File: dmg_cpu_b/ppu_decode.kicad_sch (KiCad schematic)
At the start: 69 parts

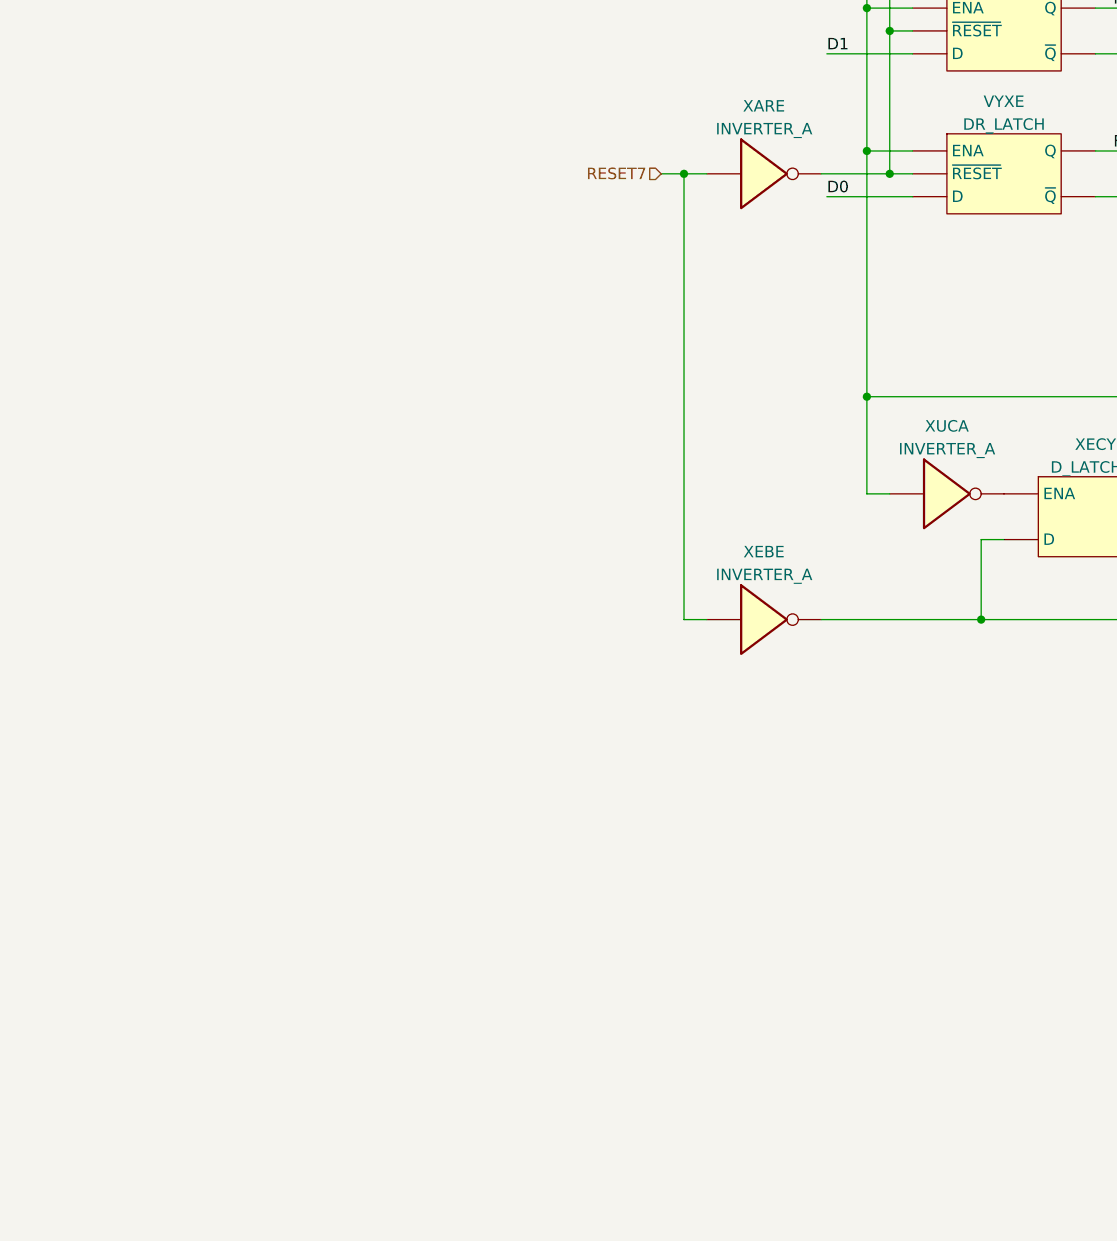
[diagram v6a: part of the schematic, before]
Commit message: PPU hierarchical page progress. Elements moved out of window sheet to be includes in BG and WIN cycles sheet
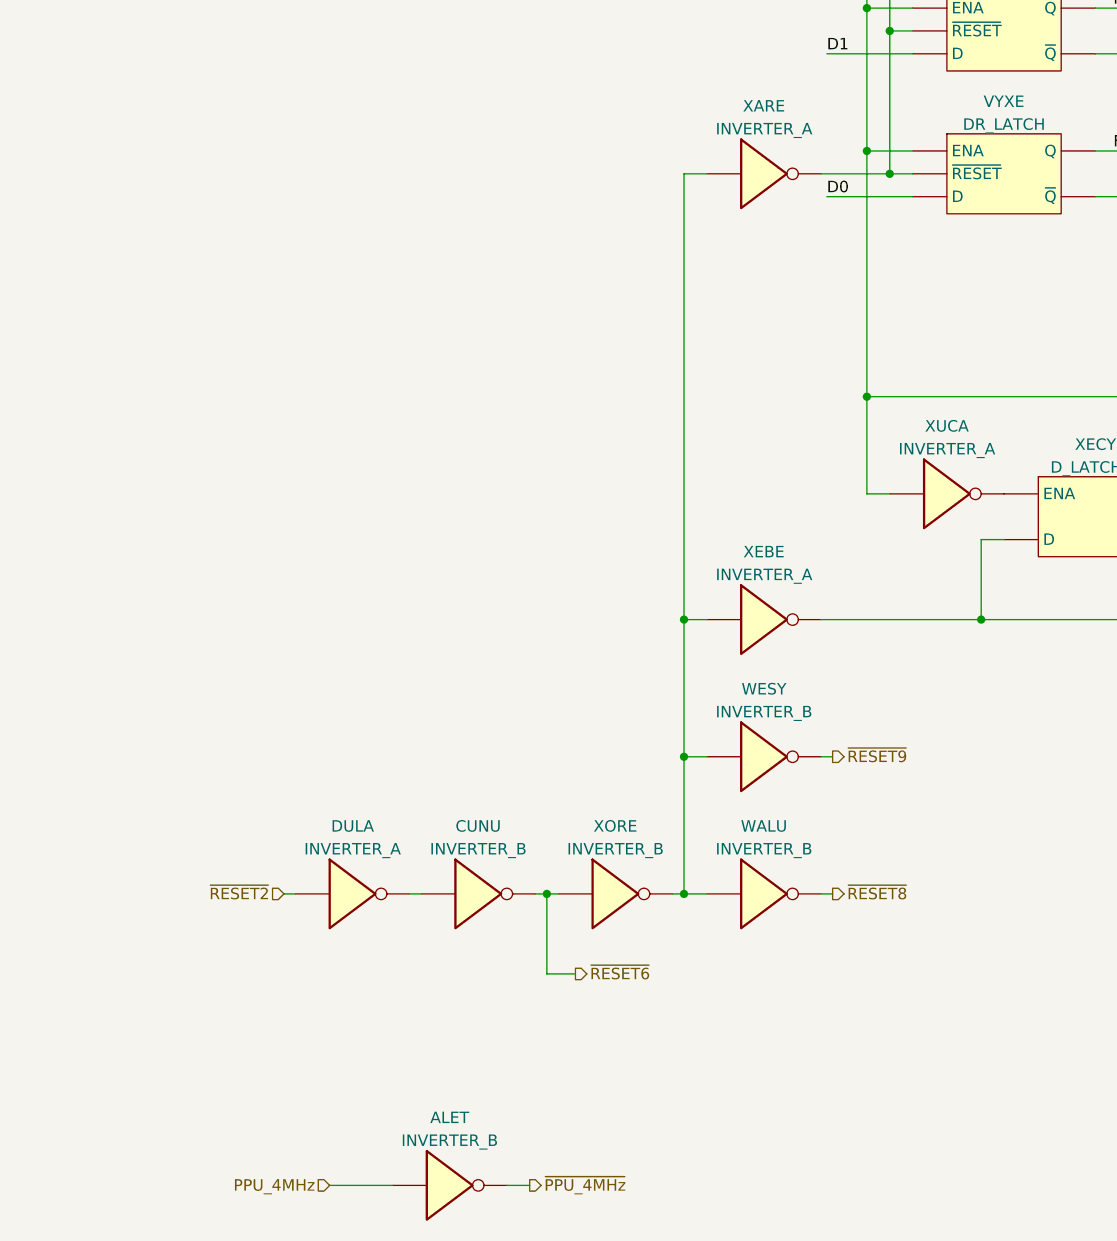
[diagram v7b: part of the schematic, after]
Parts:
- added ALET, CUNU, WALU, WESY, XORE: INVERTER_B, symbol DMG_CPU_Cells:INVERTER_B
- added DULA: INVERTER_A, symbol DMG_CPU_Cells:INVERTER_A
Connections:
- net RESET7: no longer names the net of XARE.1, XEBE.1
- net RESET7: now also WALU.1, WESY.1, XORE.2
- new net: CUNU.1, DULA.2
- new net PPU_4MHz: ALET.1
- new net ~{PPU_4MHz}: ALET.2
- new net ~{RESET2}: DULA.1
- new net ~{RESET6}: CUNU.2, XORE.1
- new net ~{RESET8}: WALU.2
- new net ~{RESET9}: WESY.2

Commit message: All connections between sheet are complete. Can still do with a good tidy up.
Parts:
- removed PYRY: INVERTER_A, symbol DMG_CPU_Cells:INVERTER_A
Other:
- moved on the sheet: AJAS, ALET, ASOT, ATAR, CUNU, CUPA, DULA, DYKY, LYFE, LYHA, TEGO, VAHA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
